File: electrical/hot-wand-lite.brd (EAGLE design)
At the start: 112 x 72 mm, 82 parts, among them IC1 12V R-78K12-2.0, IC2 AMS1117-5.0, Q1 NCHAN, Q2 SIS862ADN-T1-GE3, Q3 DMTH64M2LPDWQ-13, Q4 2N7002K, Q5 SIS862ADN-T1-GE3, U1 SEEED-XIAO-SAMD21, U2 1EDN8511BXUSA1, U3 LM74700QDBVTQ1, U4 AP53781

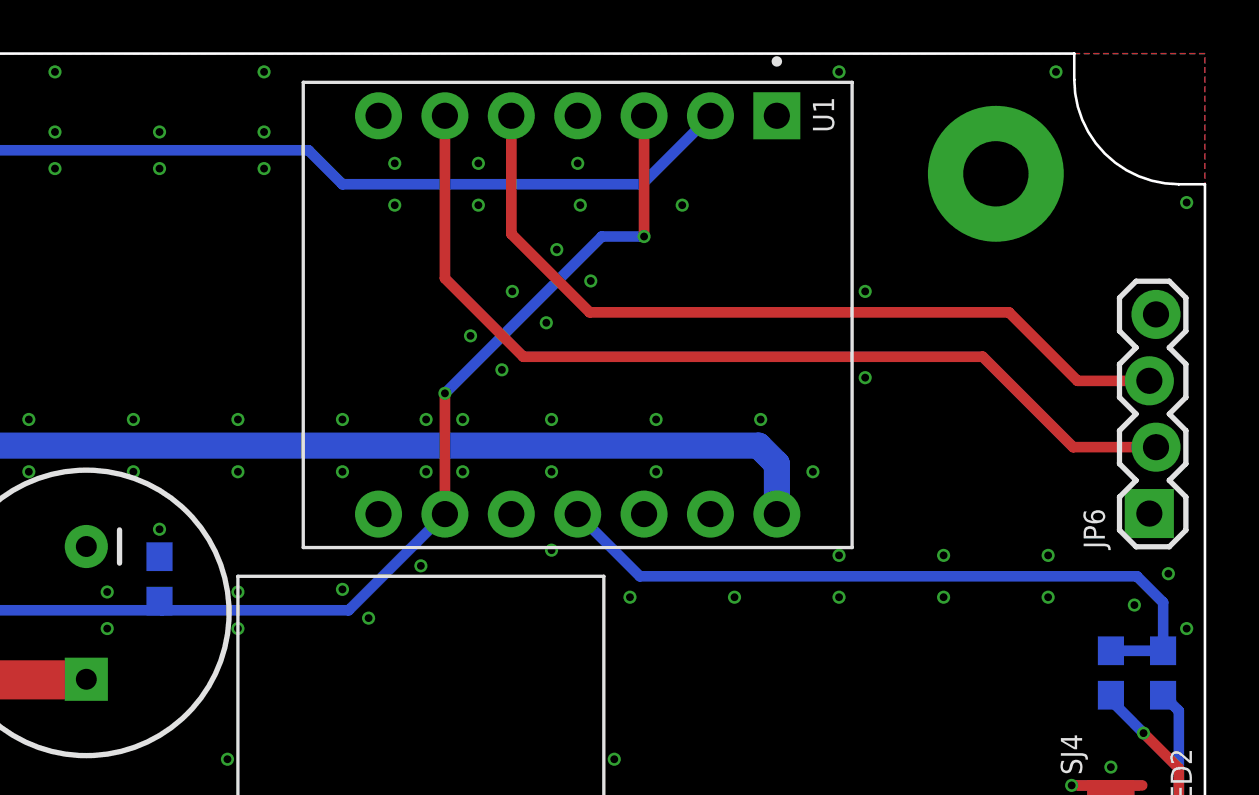
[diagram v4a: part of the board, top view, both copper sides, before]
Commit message: update lite design for locking mcu footprint
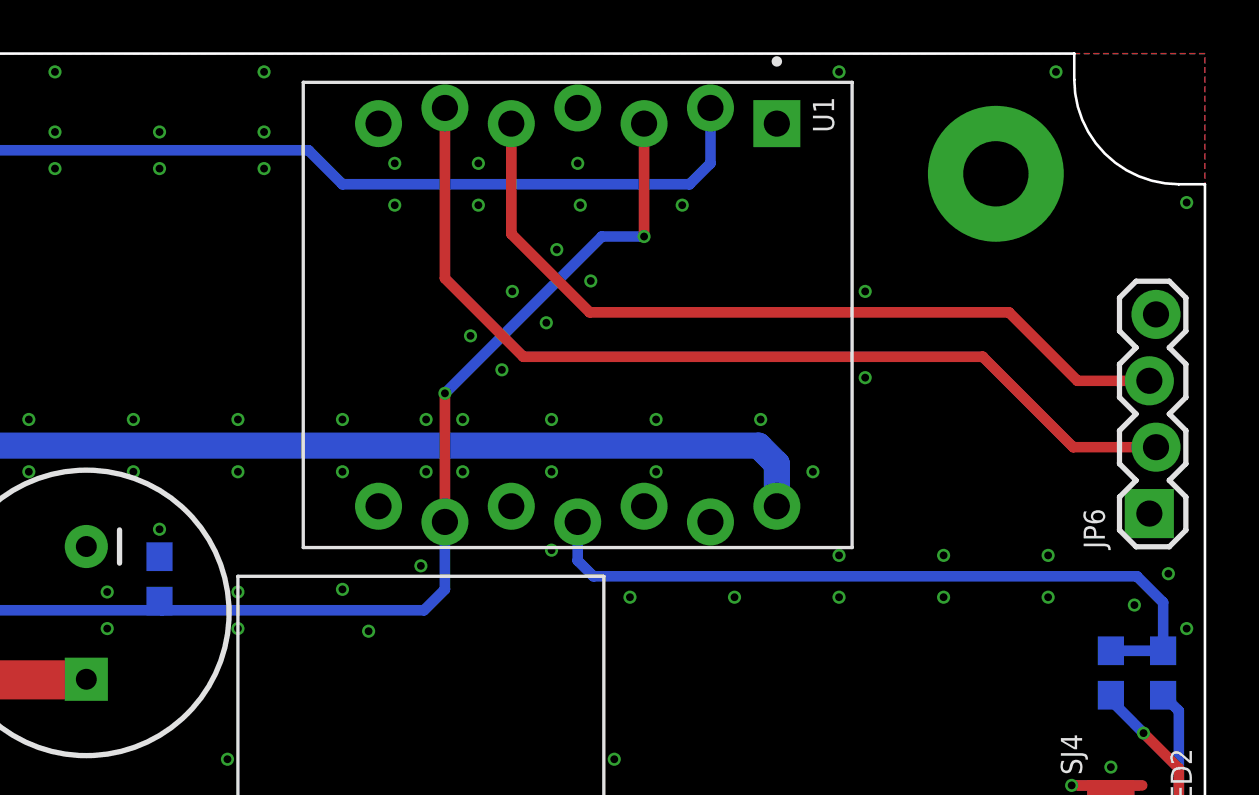
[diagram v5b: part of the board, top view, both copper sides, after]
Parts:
- U1: value SEEED-XIAO-SAMD21 -> SEEED-XIAO-SAMD21-TH-LOCKING; device hot-wand:MODULE_102010388 -> hot-wand:MODULE_102010388_LOCKING
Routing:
- net ADC: track 41.9 -> 43.3 mm
- net RF-GEN: track 32.8 -> 34.2 mm
- net LED: track 27.7 -> 28.4 mm
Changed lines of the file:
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@@
 <attribute name="PARTNUM" value="AMS1117-5.0" x="59" y="56.5" size="1.778" layer="28" rot="MR90" display="off"/>
 </element>
-<element name="U1" library="hot-wand" package="MODULE_102010388" value="SEEED-XIAO-SAMD21" x="88" y="62" smashed="yes" rot="R270">
+<element name="U1" library="hot-wand" package="MODULE_102010388_LOCKING" value="SEEED-XIAO-SAMD21-TH-LOCKING" x="88" y="62" smashed="yes" rot="R270">
 <attribute name="PRICE" value="None" x="88" y="62" size="1.778" layer="27" rot="R270" display="off"/>
 <attribute name="PURCHASE-URL" value="https://www.snapeda.com/api/url_track_click_mouser/?unipart_id=7601083&amp;manufacturer=seeed technology limited&amp;part_name=102010388&amp;search_term=xiao samd21" x="88" y="62" size="1.778" layer="27" rot="R270" display="off"/>
@@
 <via x="75" y="50" extent="1-16" drill="0.3" shape="octagon"/>
 <via x="79" y="51.5" extent="1-16" drill="0.3" shape="octagon"/>
-<via x="80" y="50.4" extent="1-16" drill="0.3" shape="octagon"/>
+<via x="80" y="49.9" extent="1-16" drill="0.3" shape="octagon"/>
 <contactref element="R22" pad="2"/>
 <via x="61.5" y="50.7" extent="1-16" drill="0.3" shape="octagon"/>
@@
 <contactref element="R1" pad="1"/>
 <contactref element="U1" pad="2"/>
-<wire x1="93.08" y1="69.62" x2="90.46" y2="67" width="0.4064" layer="16"/>
-<wire x1="90.46" y1="67" x2="79" y2="67" width="0.4064" layer="16"/>
+<wire x1="79" y1="67" x2="92.28" y2="67" width="0.4064" layer="16"/>
+<wire x1="92.28" y1="67" x2="93.08" y2="67.8" width="0.4064" layer="16"/>
+<wire x1="93.08" y1="67.8" x2="93.08" y2="69.92" width="0.4064" layer="16"/>
 <wire x1="79" y1="67" x2="77.7" y2="68.3" width="0.4064" layer="16"/>
 <wire x1="77.7" y1="68.3" x2="61.9" y2="68.3" width="0.4064" layer="16"/>
@@
 <wire x1="62.099" y1="56.5" x2="65" y2="56.5" width="1" layer="16"/>
 <wire x1="65" y1="56.5" x2="65" y2="56.4" width="1" layer="16"/>
-<wire x1="95.62" y1="54.38" x2="95.62" y2="56.299715625" width="1" layer="16"/>
+<wire x1="95.62" y1="54.68" x2="95.62" y2="56.299715625" width="1" layer="16"/>
 <wire x1="95.62" y1="56.299715625" x2="94.919715625" y2="57" width="1" layer="16"/>
 <wire x1="94.919715625" y1="57" x2="65.6" y2="57" width="1" layer="16"/>
@@
 <wire x1="104.5" y1="62.1" x2="88.46" y2="62.1" width="0.4064" layer="1"/>
 <wire x1="88.46" y1="62.1" x2="85.46" y2="65.1" width="0.4064" layer="1"/>
-<wire x1="85.46" y1="65.1" x2="85.46" y2="69.62" width="0.4064" layer="1"/>
+<wire x1="85.46" y1="65.1" x2="85.46" y2="69.32" width="0.4064" layer="1"/>
 </signal>
 <signal name="SEL2">
@@
 <wire x1="103.5" y1="60.4" x2="85.92" y2="60.4" width="0.4064" layer="1"/>
 <wire x1="85.92" y1="60.4" x2="82.92" y2="63.4" width="0.4064" layer="1"/>
-<wire x1="82.92" y1="63.4" x2="82.92" y2="69.62" width="0.4064" layer="1"/>
+<wire x1="82.92" y1="63.4" x2="82.92" y2="69.92" width="0.4064" layer="1"/>
 </signal>
 <signal name="LED">
 <contactref element="U1" pad="11"/>
 <contactref element="R5" pad="1"/>
-<wire x1="88" y1="54.38" x2="90.38" y2="52" width="0.4064" layer="16"/>
-<wire x1="90.38" y1="52" x2="109.4" y2="52" width="0.4064" layer="16"/>
+<wire x1="109.4" y1="52" x2="88.6" y2="52" width="0.4064" layer="16"/>
+<wire x1="88.6" y1="52" x2="88" y2="52.6" width="0.4064" layer="16"/>
+<wire x1="88" y1="52.6" x2="88" y2="54.08" width="0.4064" layer="16"/>
 <wire x1="109.4" y1="52" x2="110.4" y2="51" width="0.4064" layer="16"/>
 <wire x1="110.4" y1="51" x2="110.4" y2="49.15" width="0.4064" layer="16"/>
@@
 <contactref element="R22" pad="1"/>
 <contactref element="U1" pad="9"/>
-<wire x1="79.24" y1="50.7" x2="82.92" y2="54.38" width="0.4064" layer="16"/>
 <wire x1="64.35" y1="48.7" x2="64.35" y2="50.7" width="0.4064" layer="16"/>
 <wire x1="64.35" y1="50.7" x2="72.1" y2="50.7" width="0.4064" layer="16"/>
 <contactref element="C23" pad="2"/>
-<wire x1="72.1" y1="50.7" x2="79.24" y2="50.7" width="0.4064" layer="16"/>
+<wire x1="72.1" y1="50.7" x2="82.12" y2="50.7" width="0.4064" layer="16"/>
+<wire x1="82.12" y1="50.7" x2="82.92" y2="51.5" width="0.4064" layer="16"/>
+<wire x1="82.92" y1="51.5" x2="82.92" y2="54.08" width="0.4064" layer="16"/>
 <wire x1="72" y1="51.05" x2="72.1" y2="51.05" width="0.4064" layer="16"/>
 <wire x1="72.1" y1="51.05" x2="72.1" y2="50.7" width="0.4064" layer="16"/>
 <contactref element="U1" pad="3"/>
-<wire x1="90.54" y1="69.62" x2="90.54" y2="65" width="0.4064" layer="1"/>
+<wire x1="90.54" y1="69.32" x2="90.54" y2="65" width="0.4064" layer="1"/>
 <via x="90.54" y="65" extent="1-16" drill="0.3" shape="octagon"/>
 <wire x1="88.92" y1="65" x2="82.92" y2="59" width="0.4064" layer="16"/>
 <via x="82.92" y="59" extent="1-16" drill="0.3" shape="octagon"/>
-<wire x1="82.92" y1="59" x2="82.92" y2="54.38" width="0.4064" layer="1"/>
+<wire x1="82.92" y1="59" x2="82.92" y2="54.08" width="0.4064" layer="1"/>
 <wire x1="88.92" y1="65" x2="90.54" y2="65" width="0.4064" layer="16"/>
 </signal>

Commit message: added power disable signal to lite MCU
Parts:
- added JP4: (no value), hot-wand:1X02_LONGPADS
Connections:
- new net PWR-DIS: JP4.2, U1.10
- net GND: now also JP4.1
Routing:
- net PWR-DIS: track 0.00 -> 23.2 mm
- net GND: vias 337 -> 341
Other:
- board text added: "PWR-DIS"
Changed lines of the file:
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@@
 <wire x1="18.1" y1="46.2" x2="18.1" y2="45.3" width="0" layer="41"/>
 <wire x1="21.1" y1="46.5" x2="21.1" y2="45.5" width="0" layer="41"/>
+<text x="101.6" y="45.4" size="1.016" layer="25" rot="R90">PWR-DIS</text>
 </plain>
 <attributes>
@@
 <attribute name="NAME" x="17.4" y="46.3" size="0.8128" layer="25" rot="R90" align="center"/>
 </element>
+<element name="JP4" library="hot-wand" package="1X02_LONGPADS" value="" x="104" y="47" rot="R90"/>
 </elements>
 <signals>
@@
 <via x="42" y="40.9" extent="1-16" drill="0.3" shape="octagon"/>
 <via x="28.2" y="16.7" extent="1-16" drill="0.3" shape="octagon"/>
+<contactref element="JP4" pad="1"/>
+<via x="98" y="48.8" extent="1-16" drill="0.3" shape="octagon"/>
+<via x="94" y="48.8" extent="1-16" drill="0.3" shape="octagon"/>
+<via x="90" y="48.8" extent="1-16" drill="0.3" shape="octagon"/>
+<via x="85" y="49" extent="1-16" drill="0.3" shape="octagon"/>
 </signal>
 <signal name="+24V">
@@
 <wire x1="11.3" y1="36.1" x2="11.6" y2="36.1" width="0.2032" layer="16"/>
 </signal>
+<signal name="PWR-DIS">
+<contactref element="U1" pad="10"/>
+<contactref element="JP4" pad="2"/>
+<wire x1="104" y1="49.54" x2="86.26" y2="49.54" width="0.4064" layer="16"/>
+<wire x1="86.26" y1="49.54" x2="85.46" y2="50.34" width="0.4064" layer="16"/>
+<wire x1="85.46" y1="50.34" x2="85.46" y2="54.68" width="0.4064" layer="16"/>
+</signal>
 </signals>

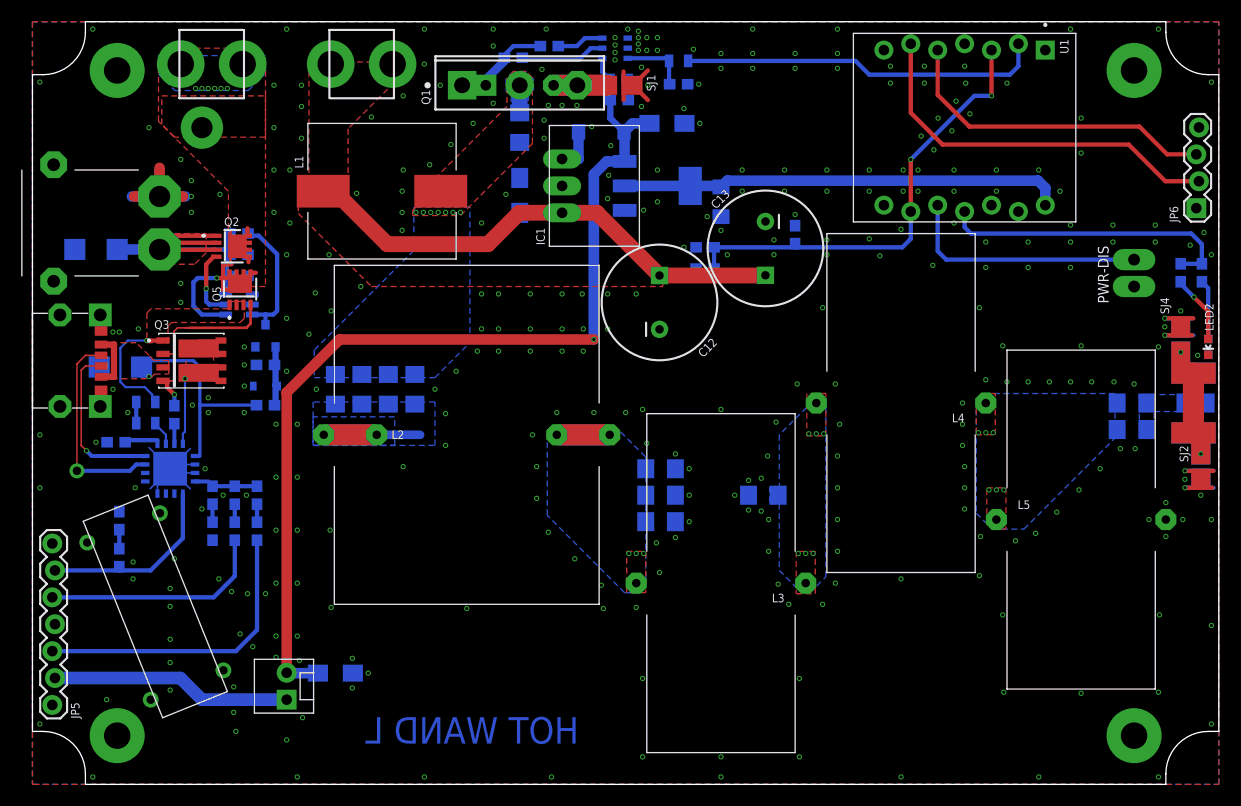
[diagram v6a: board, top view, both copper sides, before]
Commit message: lite pcb, added esd tvs diodes
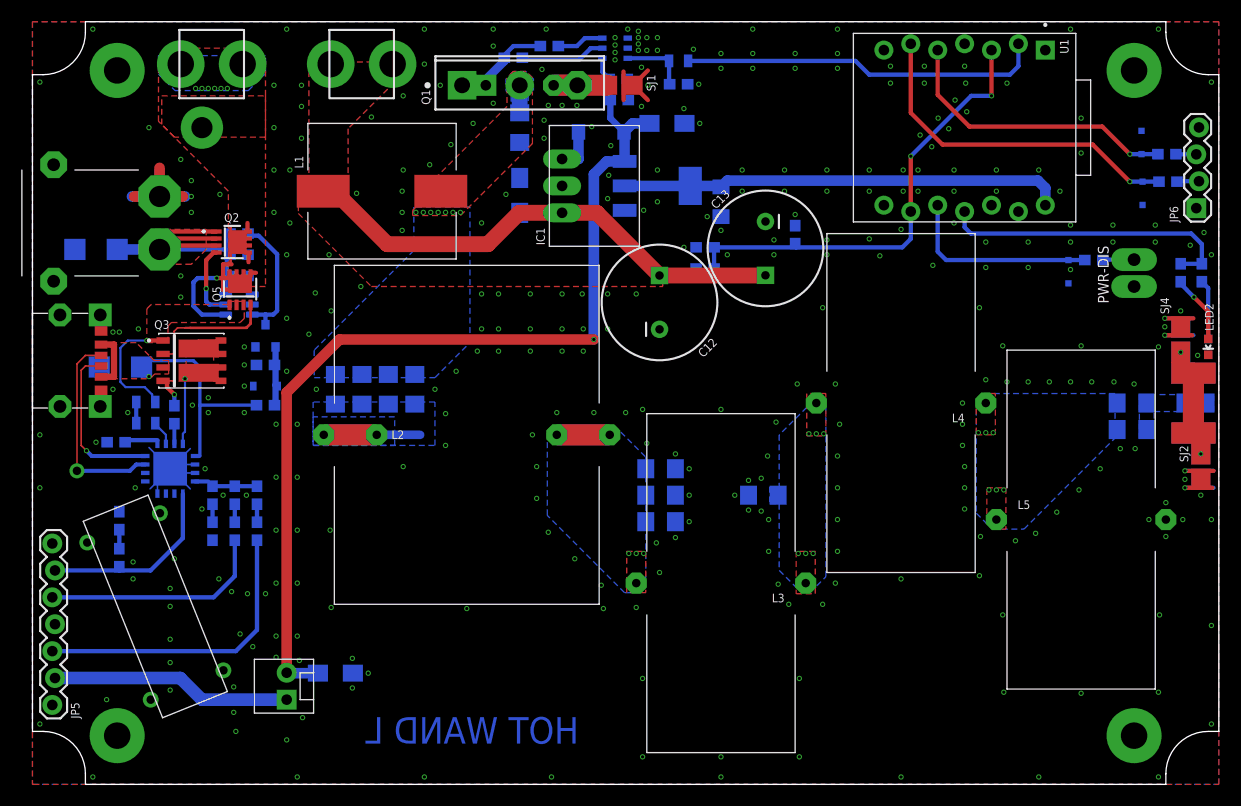
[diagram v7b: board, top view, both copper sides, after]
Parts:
- added R23, R24, R25: 470Ω, hot-wand:0603-RES
- added TVS4, TVS5, TVS6: (no value), hot-wand:SOD323-R
- moved Q2 0.40 mm to (18.8, 51.2)
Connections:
- new net N$17: JP6.2, R23.2
- new net N$18: JP6.3, R24.2
- new net N$21: JP4.2, R25.2
- net GND: now also TVS4.A, TVS5.A, TVS6.A
- net PWR-DIS: now also R25.1, TVS6.C; no longer JP4.2
- net SEL2: now also R23.1, TVS4.C; no longer JP6.2
- net SEL3: now also R24.1, TVS5.C; no longer JP6.3
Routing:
- net PWR-DIS: track 23.2 -> 18.6 mm
- net SEL2: track 36.4 -> 32.6 mm, vias 0 -> 1
- net SEL3: track 31.0 -> 27.3 mm, vias 0 -> 1
- net N$21: track 0.00 -> 2.97 mm
- net N$17: track 0.00 -> 2.09 mm
- net N$18: track 0.00 -> 1.93 mm
- net DC-SRC: track 18.6 -> 19.5 mm
